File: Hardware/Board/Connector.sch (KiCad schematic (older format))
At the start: 0 parts

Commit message: Wago und FPC Libs zugefügt
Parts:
- added J?: WAGO_Klemmleiste_4-pol, symbol WAGO~Klemmleisten:WAGO_Klemmleiste_4-pol
- added J? (x2): WAGO_Klemmleiste_8-pol, symbol WAGO~Klemmleisten:WAGO_Klemmleiste_8-pol
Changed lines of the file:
@@
 Comment4 ""
 $EndDescr
+$Comp
+L WAGO~Klemmleisten:WAGO_Klemmleiste_4-pol J?
+U 1 1 5CB5F9FC
+P 2900 1300
+F 0 "J?" H 2979 1292 50  0000 L CNN
+F 1 "WAGO_Klemmleiste_4-pol" H 2979 1201 50  0000 L CNN
+F 2 "" H 2900 1300 50  0001 C CNN
+F 3 "~" H 2900 1300 50  0001 C CNN
+	1    2900 1300
+	1    0    0    -1
+$EndComp
+$Comp
+L WAGO~Klemmleisten:WAGO_Klemmleiste_8-pol J?
+U 1 1 5CB5FBA8
+P 2900 2050
+F 0 "J?" H 2979 2042 50  0000 L CNN
+F 1 "WAGO_Klemmleiste_8-pol" H 2979 1951 50  0000 L CNN
+F 2 "" H 2900 2050 50  0001 C CNN
+F 3 "~" H 2900 2050 50  0001 C CNN
+	1    2900 2050
+	1    0    0    -1
+$EndComp
+$Comp
+L WAGO~Klemmleisten:WAGO_Klemmleiste_8-pol J?
+U 1 1 5CB5FC2E
+P 2900 3000
+F 0 "J?" H 2979 2992 50  0000 L CNN
+F 1 "WAGO_Klemmleiste_8-pol" H 2979 2901 50  0000 L CNN
+F 2 "" H 2900 3000 50  0001 C CNN
+F 3 "~" H 2900 3000 50  0001 C CNN
+	1    2900 3000
+	1    0    0    -1
+$EndComp
 $EndSCHEMATC

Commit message: Netzliste und Board erstellt, hier sind noch Fehler im Bereich Footprints, BLE Modul nRF8001 hinzugefügt, erste Anschlussklemmen zugefügt
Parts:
- added J11: RJ12, symbol Connector:RJ12
- added J12: RJ45, symbol Connector:RJ45
- added J13, J7: WAGO_Klemmleiste_6-pol, TerminalBlock_WAGO:TerminalBlock_WAGO_236-106_1x06_P5.00mm_45Degree, symbol WAGO~Klemmleisten:WAGO_Klemmleiste_6-pol
- J10, J9: renamed from J?; footprint (none) -> TerminalBlock_WAGO:TerminalBlock_WAGO_236-108_1x08_P5.00mm_45Degree
- J8: renamed from J?; footprint (none) -> TerminalBlock_WAGO:TerminalBlock_WAGO_236-304_1x04_P10.00mm_45Degree
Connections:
- net labels added: 1Wire_P0, 1Wire_P1, 1Wire_P2, 1Wire_P3, 1Wire_P4, 1Wire_P5, 1Wire_P6, 1Wire_P7, CAN-H, CAN-L, DC_Input, GND, LIN1, LIN2, LIN3, RS485-A, RS485-B
- wire segments 0 -> 65
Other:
- note added: "1Wire Sensors 1-4"
- note added: "1Wire Sensors 5-8"
- note added: "CAN & RS485"
- note added: "Dormetic Klima"
- note added: "LIN-Bus connections"
- note added: "Power"
- note added: "TI-Bus"
- note added: "Truma"

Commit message: Eine Menge Arbeit auf der GPN, fast fertig im Schaltplan.
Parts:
- J10, J9: symbol WAGO~Klemmleisten:WAGO_Klemmleiste_8-pol -> Womo-rescue:WAGO_Klemmleiste_8-pol-WAGO_Klemmleisten
- J13, J7: symbol WAGO~Klemmleisten:WAGO_Klemmleiste_6-pol -> Womo-rescue:WAGO_Klemmleiste_6-pol-WAGO_Klemmleisten
- J8: symbol WAGO~Klemmleisten:WAGO_Klemmleiste_4-pol -> Womo-rescue:WAGO_Klemmleiste_4-pol-WAGO_Klemmleisten
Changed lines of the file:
@@
 EESchema Schematic File Version 4
 LIBS:Womo-cache
-EELAYER 26 0
+EELAYER 29 0
 EELAYER END
 $Descr A4 11693 8268
 encoding utf-8
-Sheet 7 7
+Sheet 6 7
 Title ""
 Date ""
@@
 $EndDescr
 $Comp
-L WAGO~Klemmleisten:WAGO_Klemmleiste_4-pol J8
+L Womo-rescue:WAGO_Klemmleiste_4-pol-WAGO_Klemmleisten J8
 U 1 1 5CB5F9FC
 P 1900 950
@@
 $EndComp
 $Comp
-L WAGO~Klemmleisten:WAGO_Klemmleiste_8-pol J9
+L Womo-rescue:WAGO_Klemmleiste_8-pol-WAGO_Klemmleisten J9
 U 1 1 5CB5FBA8
 P 1900 2050
@@
 $EndComp
 $Comp
-L WAGO~Klemmleisten:WAGO_Klemmleiste_8-pol J10
+L Womo-rescue:WAGO_Klemmleiste_8-pol-WAGO_Klemmleisten J10
 U 1 1 5CB5FC2E
 P 1900 3450
@@
 $EndComp
 $Comp
-L WAGO~Klemmleisten:WAGO_Klemmleiste_6-pol J7
+L Womo-rescue:WAGO_Klemmleiste_6-pol-WAGO_Klemmleisten J7
 U 1 1 5CBD1756
 P 1850 5700
@@
 	700  600  700  1450
 $Comp
-L WAGO~Klemmleisten:WAGO_Klemmleiste_6-pol J13
+L Womo-rescue:WAGO_Klemmleiste_6-pol-WAGO_Klemmleisten J13
 U 1 1 5CBE3A31
 P 5250 1050

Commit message: Board to Board Verbindung eingefügt
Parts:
- added J2: Conn_02x25_Odd_Even, Connector_PinSocket_2.54mm:PinSocket_2x25_P2.54mm_Vertical, symbol Connector_Generic:Conn_02x25_Odd_Even
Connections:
- net GND: now also J2.1 (Pin_1), J2.2 (Pin_2), J2.23 (Pin_23), J2.24 (Pin_24), J2.33 (Pin_33), J2.34 (Pin_34), J2.43 (Pin_43), J2.44 (Pin_44), J2.49 (Pin_49), J2.50 (Pin_50)
- new net +3.3VA: J2.36 (Pin_36), J2.38 (Pin_38)
- new net +3V3: J2.39 (Pin_39), J2.41 (Pin_41)
- new net +VSW: J2.40 (Pin_40), J2.42 (Pin_42)
- new net M_CAN1_RX: J2.11 (Pin_11)
- new net M_CAN1_TX: J2.9 (Pin_9)
- new net M_ESP_Boot: J2.29 (Pin_29)
- new net M_ESP_Enable: J2.27 (Pin_27)
- new net M_ESP_Reset: J2.25 (Pin_25)
- new net M_I2C2_SCL: J2.13 (Pin_13)
- new net M_I2C2_SDA: J2.15 (Pin_15)
- new net M_I2C4_SCL: J2.17 (Pin_17)
- new net M_I2C4_SDA: J2.19 (Pin_19)
- new net M_LCD_LED-A: J2.46 (Pin_46), J2.48 (Pin_48)
- new net M_LCD_LED-K: J2.45 (Pin_45), J2.47 (Pin_47)
- new net M_LPUART_RTS_DE_RS485: J2.7 (Pin_7)
- new net M_LPUART_RX_RX485: J2.5 (Pin_5)
- new net M_LPUART_TX_RS485: J2.3 (Pin_3)
- new net M_PA9: J2.31 (Pin_31)
- new net M_PB2: J2.32 (Pin_32)
- new net M_PF11: J2.30 (Pin_30)
- new net M_PWR_Reset: J2.21 (Pin_21)
- new net M_Rasp_Shutdown: J2.26 (Pin_26)
- new net M_Rasp_down: J2.28 (Pin_28)
- new net M_UART4_RX: J2.18 (Pin_18)
- new net M_UART4_TX: J2.16 (Pin_16)
- new net M_UART5_RX: J2.22 (Pin_22)
- new net M_UART5_TX: J2.20 (Pin_20)
- new net M_USART1_RX_LIN1: J2.6 (Pin_6)
- new net M_USART1_TX_LIN1: J2.4 (Pin_4)
- new net M_USART2_RX_LIN2: J2.10 (Pin_10)
- new net M_USART2_TX_LIN2: J2.8 (Pin_8)
- new net M_USART3_RX_LIN3: J2.14 (Pin_14)
- new net M_USART3_TX_LIN3: J2.12 (Pin_12)

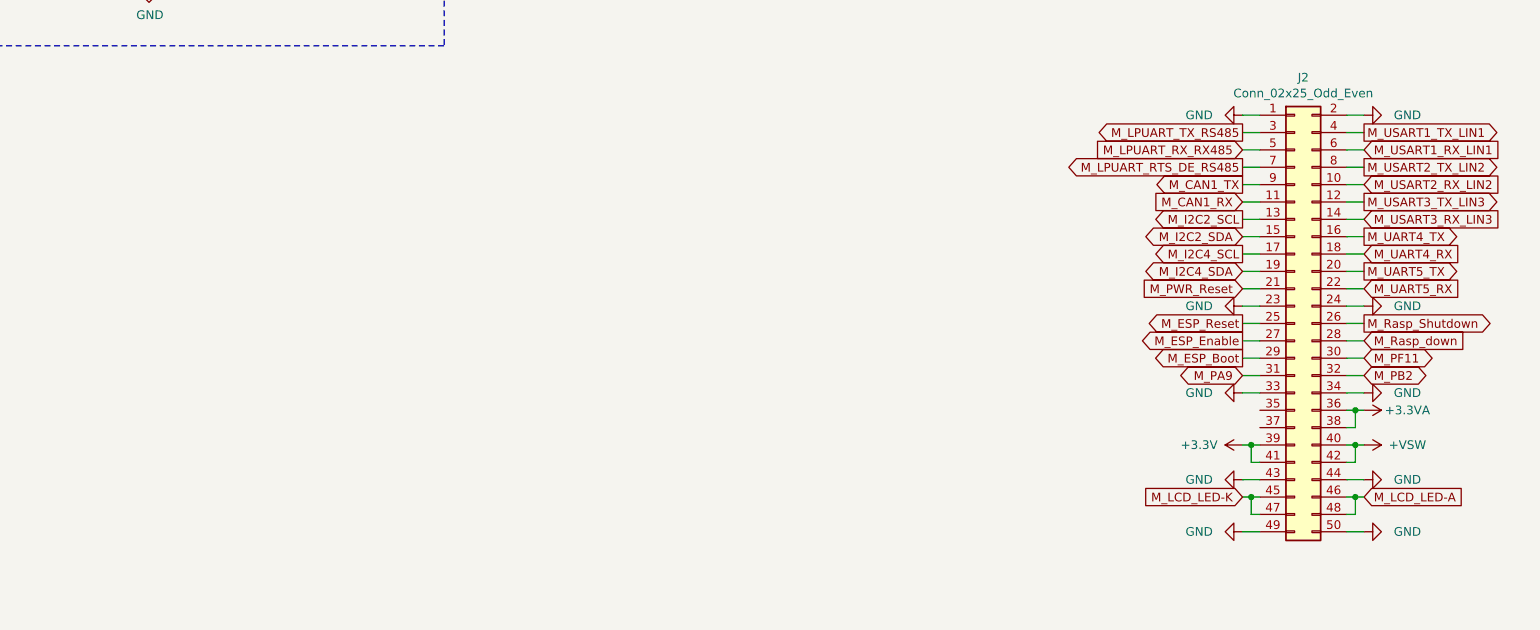
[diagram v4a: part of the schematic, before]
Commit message: Resitiven Touch Controller eingefügt, diverse I2C Parts hinzu gefügt, Netze umgenannt
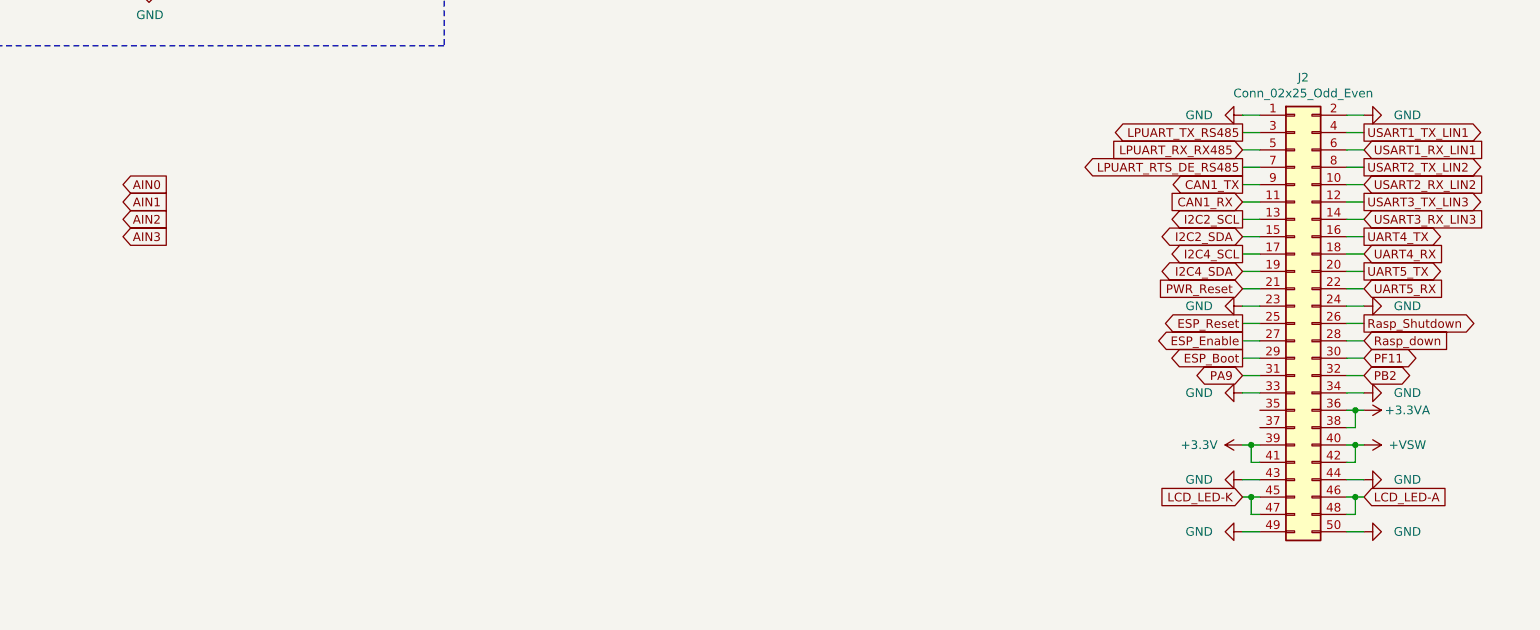
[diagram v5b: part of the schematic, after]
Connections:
- net M_CAN1_RX renamed CAN1_RX
- net M_CAN1_TX renamed CAN1_TX
- net M_ESP_Boot renamed ESP_Boot
- net M_ESP_Enable renamed ESP_Enable
- net M_ESP_Reset renamed ESP_Reset
- net M_I2C2_SCL renamed I2C2_SCL
- net M_I2C2_SDA renamed I2C2_SDA
- net M_I2C4_SCL renamed I2C4_SCL
- net M_I2C4_SDA renamed I2C4_SDA
- net M_LCD_LED-A renamed LCD_LED-A
- net M_LCD_LED-K renamed LCD_LED-K
- net M_LPUART_RTS_DE_RS485 renamed LPUART_RTS_DE_RS485
- net M_LPUART_RX_RX485 renamed LPUART_RX_RX485
- net M_LPUART_TX_RS485 renamed LPUART_TX_RS485
- net M_PA9 renamed PA9
- net M_PB2 renamed PB2
- net M_PF11 renamed PF11
- net M_PWR_Reset renamed PWR_Reset
- net M_Rasp_Shutdown renamed Rasp_Shutdown
- net M_Rasp_down renamed Rasp_down
- net M_UART4_RX renamed UART4_RX
- net M_UART4_TX renamed UART4_TX
- net M_UART5_RX renamed UART5_RX
- net M_UART5_TX renamed UART5_TX
- net M_USART1_RX_LIN1 renamed USART1_RX_LIN1
- net M_USART1_TX_LIN1 renamed USART1_TX_LIN1
- net M_USART2_RX_LIN2 renamed USART2_RX_LIN2
- net M_USART2_TX_LIN2 renamed USART2_TX_LIN2
- net M_USART3_RX_LIN3 renamed USART3_RX_LIN3
- net M_USART3_TX_LIN3 renamed USART3_TX_LIN3
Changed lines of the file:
@@
 $EndComp
 Text GLabel 11200 2700 0    50   Input ~ 0
-M_CAN1_RX
+CAN1_RX
 Text GLabel 11200 2600 0    50   Output ~ 0
-M_CAN1_TX
+CAN1_TX
 Text GLabel 11200 2400 0    50   Input ~ 0
-M_LPUART_RX_RX485
+LPUART_RX_RX485
 Text GLabel 11200 2300 0    50   Output ~ 0
-M_LPUART_TX_RS485
+LPUART_TX_RS485
 Text GLabel 11200 2500 0    50   Output ~ 0
-M_LPUART_RTS_DE_RS485
+LPUART_RTS_DE_RS485
 Text GLabel 11200 2900 0    50   BiDi ~ 0
-M_I2C2_SDA
+I2C2_SDA
 Text GLabel 11200 2800 0    50   Output ~ 0
-M_I2C2_SCL
+I2C2_SCL
 Text GLabel 11200 3600 0    50   Output ~ 0
-M_ESP_Boot
+ESP_Boot
 Text GLabel 11200 3400 0    50   Output ~ 0
-M_ESP_Reset
+ESP_Reset
 Text GLabel 11200 3500 0    50   Output ~ 0
-M_ESP_Enable
+ESP_Enable
 Text GLabel 11200 3100 0    50   BiDi ~ 0
-M_I2C4_SDA
+I2C4_SDA
 Text GLabel 11200 3000 0    50   Output ~ 0
-M_I2C4_SCL
+I2C4_SCL
 $Comp
 L power:+3.3V #PWR?
@@
 $EndComp
 Text GLabel 11200 4400 0    50   Input ~ 0
-M_LCD_LED-K
+LCD_LED-K
 Text GLabel 11200 3200 0    50   Input ~ 0
-M_PWR_Reset
+PWR_Reset
 $Comp
 L power:GND #PWR?
@@
 	11200 4300 11300 4300
 Text GLabel 11900 2400 2    50   Input ~ 0
-M_USART1_RX_LIN1
+USART1_RX_LIN1
 Text GLabel 11900 2300 2    50   Output ~ 0
-M_USART1_TX_LIN1
+USART1_TX_LIN1
 Text GLabel 11900 3400 2    50   Output ~ 0
-M_Rasp_Shutdown
+Rasp_Shutdown
 Text GLabel 11900 3500 2    50   Input ~ 0
-M_Rasp_down
+Rasp_down
 Text GLabel 11900 3100 2    50   Output ~ 0
-M_UART5_TX
+UART5_TX
 Text GLabel 11900 2700 2    50   Output ~ 0
-M_USART3_TX_LIN3
+USART3_TX_LIN3
 Text GLabel 11900 2800 2    50   Input ~ 0
-M_USART3_RX_LIN3
+USART3_RX_LIN3
 Text GLabel 11900 3200 2    50   Input ~ 0
-M_UART5_RX
+UART5_RX
 Text GLabel 11900 2600 2    50   Input ~ 0
-M_USART2_RX_LIN2
+USART2_RX_LIN2
 Text GLabel 11900 2500 2    50   Output ~ 0
-M_USART2_TX_LIN2
+USART2_TX_LIN2
 Text GLabel 11900 2900 2    50   Output ~ 0
-M_UART4_TX
+UART4_TX
 Text GLabel 11900 3000 2    50   Input ~ 0
-M_UART4_RX
+UART4_RX
 $Comp
 L power:GND #PWR?
@@
 $EndComp
 Text GLabel 11900 4400 2    50   Input ~ 0
-M_LCD_LED-A
+LCD_LED-A
 $Comp
 L power:GND #PWR?
@@
 $EndComp
 Text GLabel 11900 3600 2    50   BiDi ~ 0
-M_PF11
+PF11
 Text GLabel 11900 3700 2    50   BiDi ~ 0
-M_PB2
+PB2
 Text GLabel 11200 3700 0    50   BiDi ~ 0
-M_PA9
+PA9
 Wire Wire Line
 	11200 2200 11300 2200
@@
 Wire Wire Line
 	11200 3800 11300 3800
+Text GLabel 4750 2600 2    50   Input ~ 0
+AIN0
+Text GLabel 4750 2700 2    50   Input ~ 0
+AIN1
+Text GLabel 4750 2800 2    50   Input ~ 0
+AIN2
+Text GLabel 4750 2900 2    50   Input ~ 0
+AIN3
 $EndSCHEMATC

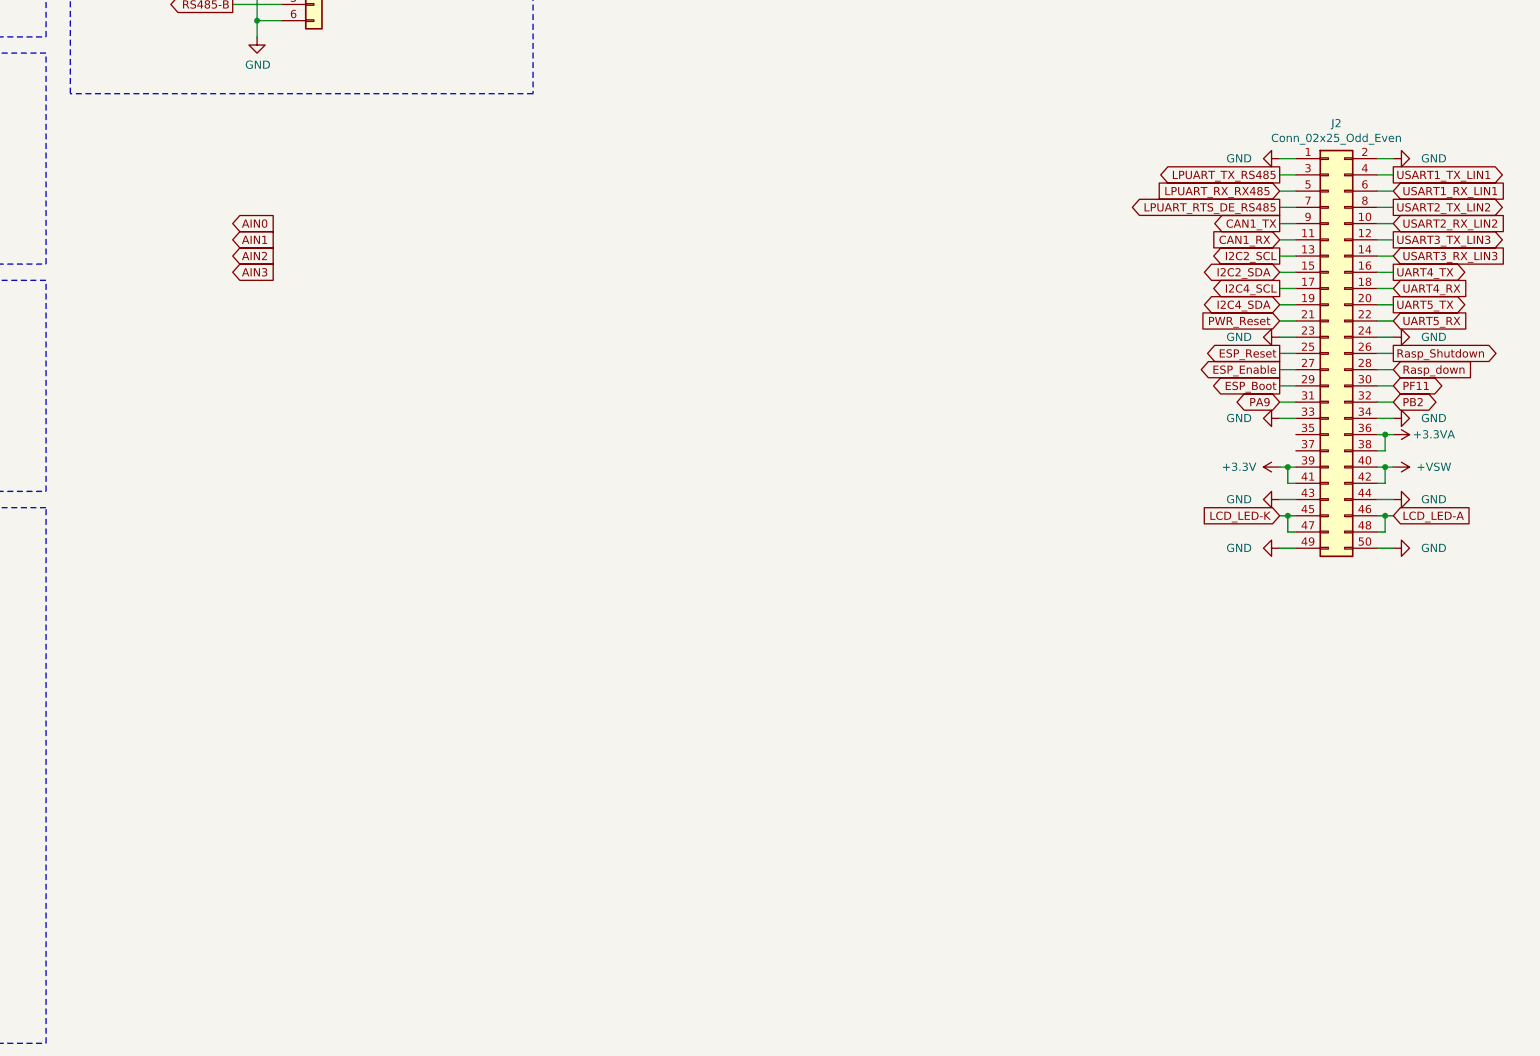
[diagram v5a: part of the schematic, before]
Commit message: GSM Modul SIM800L eingefügt, Spannung MCU Board umgenannt
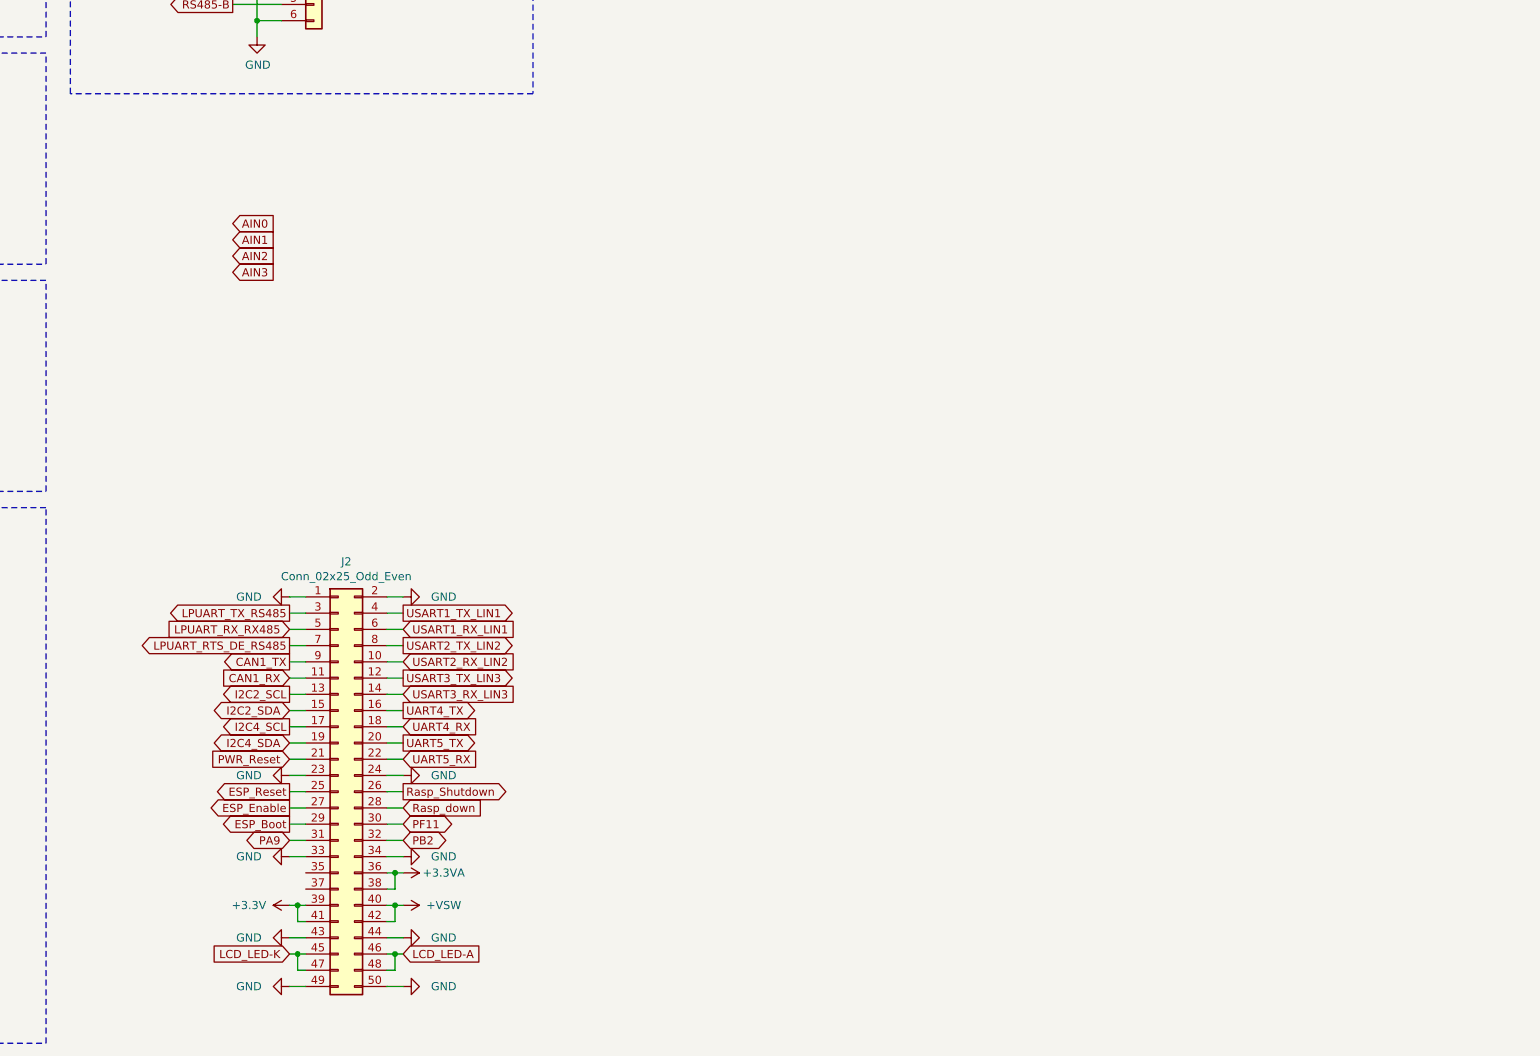
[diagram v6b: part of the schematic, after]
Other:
- moved on the sheet: J2
